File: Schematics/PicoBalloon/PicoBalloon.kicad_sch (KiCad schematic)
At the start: 31 parts, among them J2 SOLAR_L, J3 SOLAR_R, J4 LORA_ANT, J5 SWD, U1 STM32F103C8Tx, U3 TMP235A4DCKR

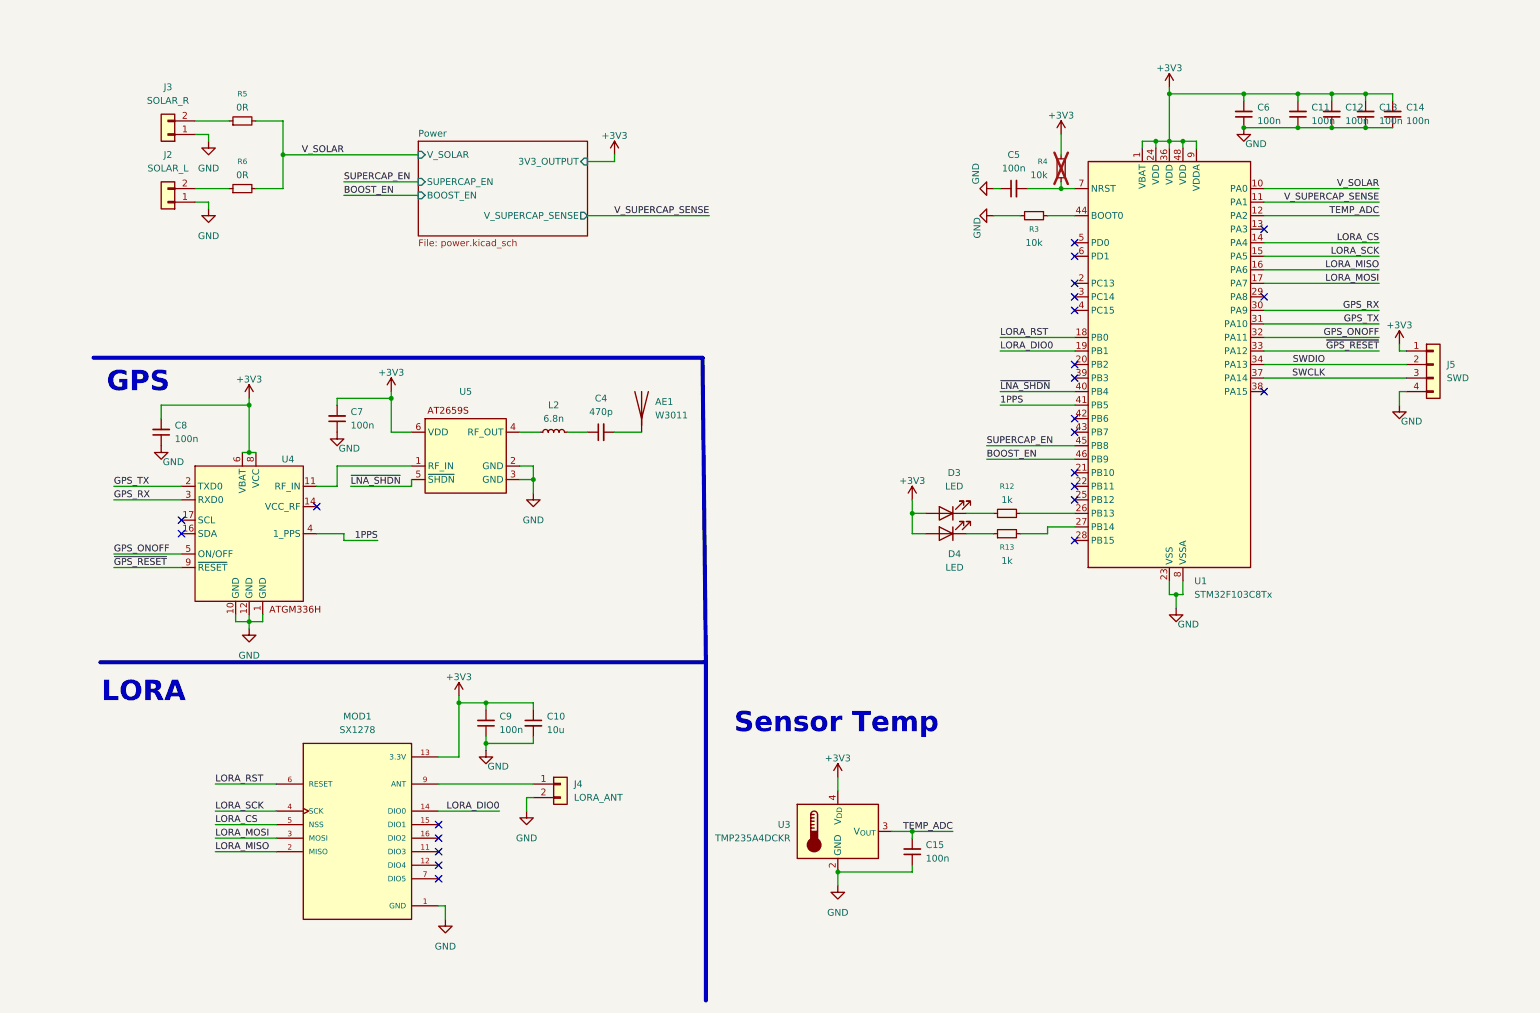
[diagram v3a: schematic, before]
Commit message: Updated R10 size and datasheets
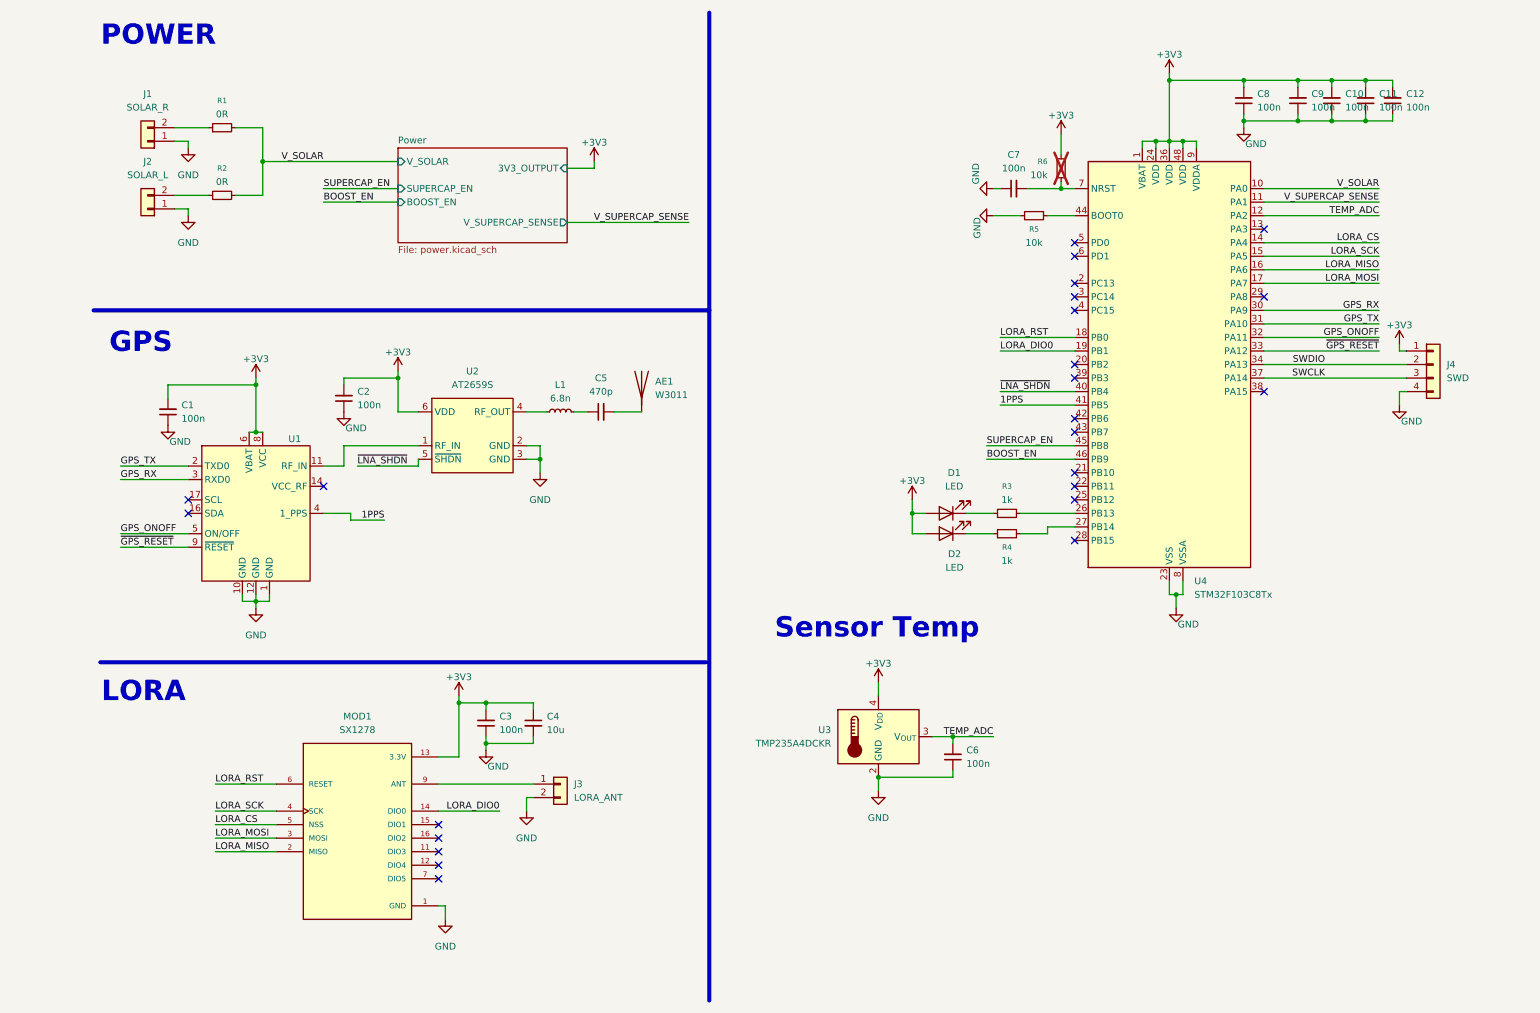
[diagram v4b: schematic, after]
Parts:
- removed U5: ~, symbol gluonLibrary:AT2659S
- added U2: AT2659S, Package_TO_SOT_SMD:SOT-23-6_Handsoldering, symbol gluonLibrary:AT2659S
- U1: renamed from U4; value ~ -> ATGM336H; footprint (none) -> GluonLib:ATGM336H; LCSC (none) -> https://lcsc.com/product-detail/GNSS-Modules_ZHONGKEWEI-ATG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
- renumbered C8 to C1, C12 to C10, C13 to C11, C14 to C12, C7 to C2, C9 to C3, C10 to C4, C4 to C5, C15 to C6, C5 to C7, C6 to C8, C11 to C9, D3 to D1, D4 to D2, J3 to J1, J4 to J3, J5 to J4, L2 to L1, R5 to R1, R6 to R2, R12 to R3, R13 to R4, R3 to R5, R4 to R6, U1 to U4
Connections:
- net +3V3: now also U2.6 (VDD)
- net GND: now also U2.2 (GND), U2.3 (GND)
- net ~{LNA_SHDN}: now also U2.5 (~{SHDN})
- net at U1.11 (RF_IN): now also U2.1 (RF_IN)
- net at L1.1: now also U2.4 (RF_OUT)
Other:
- note added: "POWER"
- moved on the sheet: AE1, C1, C10, C11, C12, C2, C5, C6, C8, C9, J1, J2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

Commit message: Fixed footprints and schematic symbols
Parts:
- removed AE1: W3011, RF_Antenna:Pulse_W3011, symbol Device:Antenna
- added AE1: Antenna_Chip, RF_Antenna:Pulse_W3011, symbol Device:Antenna_Chip
- MOD1: footprint GluonLib:SX1278_XCVR_RFM98W-433S2 -> GluonLib:SX1278
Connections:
- net GND: now also AE1.1 (FEED)
- net at C5.2: now also AE1.2 (PCB_Trace)
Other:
- note added: "Temp Sensor"
- note removed: "Sensor Temp"
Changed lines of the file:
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@@
 	(generator_version "9.0")
 	(paper "A4")
-	(text "Sensor Temp"
+	(text "Temp Sensor"
 		(exclude_from_sim no)
 		(at 158.496 128.27 0)
@@
 	(wire
 		(pts
+			(xy 119.38 87.63) (xy 119.38 88.9)
+		)
+		(stroke
+			(width 0)
+			(type default)
+		)
+	)
+	(wire
+		(pts
 			(xy 92.71 162.56) (xy 92.71 160.02)
 		)
@@
 	)
 	(symbol
+		(lib_id "Device:Antenna_Chip")
+		(at 116.84 85.09 0)
+		(mirror y)
+		(unit 1)
+		(exclude_from_sim no)
+		(in_bom yes)
+		(on_board yes)
+		(dnp no)
+		(fields_autoplaced yes)
+		(property "Reference" "AE1"
+			(at 116.205 73.66 0)
+			(effects
+				(font
+					(size 1.27 1.27)
+				)
+			)
+		)
+		(property "Value" "Antenna_Chip"
+			(at 116.205 76.2 0)
+			(effects
+				(font
+					(size 1.27 1.27)
+				)
+			)
+		)
+		(property "Footprint" "RF_Antenna:Pulse_W3011"
+			(at 119.38 80.645 0)
+			(effects
+				(font
+					(size 1.27 1.27)
+				)
+				(hide yes)
+			)
+		)
+		(property "Datasheet" "~"
+			(at 119.38 80.645 0)
+			(effects
+				(font
+					(size 1.27 1.27)
+				)
+				(hide yes)
+			)
+		)
+		(property "Description" "Ceramic chip antenna with pin for PCB trace"
+			(at 116.84 85.09 0)
+			(effects
+				(font
+					(size 1.27 1.27)
+				)
+				(hide yes)
+			)
+		)
+		(property "LCSC" "https://lcsc.com/product-detail/Antennas_PULSE-W3011_C6604735.html"
+			(at 116.84 85.09 0)
+			(effects
+				(font
+					(size 1.27 1.27)
+				)
+				(hide yes)
+			)
+		)
+		(pin "1"
+		)
+		(pin "2"
+		)
+		(instances
+			(project ""
+				(path "/0b983980-f4cd-49d3-aecb-9bdb75de805b"
+					(reference "AE1")
+					(unit 1)
+				)
+			)
+		)
+	)
+	(symbol
 		(lib_id "power:GND")
 		(at 95.25 99.06 0)
@@
 	)
 	(symbol
+		(lib_id "power:GND")
+		(at 119.38 88.9 0)
+		(unit 1)
+		(exclude_from_sim no)
+		(in_bom yes)
+		(on_board yes)
+		(dnp no)
+		(fields_autoplaced yes)
+		(property "Reference" "#PWR031"
+			(at 119.38 95.25 0)
+			(effects
+				(font
+					(size 1.27 1.27)
+				)
+				(hide yes)
+			)
+		)
+		(property "Value" "GND"
+			(at 119.38 93.98 0)
+			(effects
+				(font
+					(size 1.27 1.27)
+				)
+			)
+		)
+		(property "Footprint" ""
+			(at 119.38 88.9 0)
+			(effects
+				(font
+					(size 1.27 1.27)
+				)
+				(hide yes)
+			)
+		)
+		(property "Datasheet" ""
+			(at 119.38 88.9 0)
+			(effects
+				(font
+					(size 1.27 1.27)
+				)
+				(hide yes)
+			)
+		)
+		(property "Description" "Power symbol creates a global label with name \"GND\" , ground"
+			(at 119.38 88.9 0)
+			(effects
+				(font
+					(size 1.27 1.27)
+				)
+				(hide yes)
+			)
+		)
+		(pin "1"
+		)
+		(instances
+			(project "PicoBalloon"
+				(path "/0b983980-f4cd-49d3-aecb-9bdb75de805b"
+					(reference "#PWR031")
+					(unit 1)
+				)
+			)
+		)
+	)
+	(symbol
 		(lib_id "Device:C_Small")
 		(at 106.68 87.63 90)
@@
 			)
 		)
-		(property "Footprint" "GluonLib:SX1278_XCVR_RFM98W-433S2"
+		(property "Footprint" "GluonLib:SX1278"
 			(at 60.96 167.64 0)
 			(effects
@@
 					(unit 1)
 				)
-			)
-		)
-	)
-	(symbol
-		(lib_id "Device:Antenna")
-		(at 114.3 82.55 0)
-		(unit 1)
-		(exclude_from_sim no)
-		(in_bom yes)
-		(on_board yes)
-		(dnp no)
-		(fields_autoplaced yes)
-		(property "Reference" "AE1"
-			(at 116.84 81.9149 0)
-			(effects
-				(font
-					(size 1.27 1.27)
-				)
-				(justify left)
-			)
-		)
-		(property "Value" "W3011"
-			(at 116.84 84.4549 0)
-			(effects
-				(font
-					(size 1.27 1.27)
-				)
-				(justify left)
-			)
-		)
-		(property "Footprint" "RF_Antenna:Pulse_W3011"
-			(at 114.3 82.55 0)
-			(effects
-				(font
-					(size 1.27 1.27)
-				)
-				(hide yes)
-			)
-		)
-		(property "Datasheet" "~"
-			(at 114.3 82.55 0)
-			(effects
-				(font
-					(size 1.27 1.27)
-				)
-				(hide yes)
-			)
-		)
-		(property "Description" "Antenna"
-			(at 114.3 82.55 0)
-			(effects
-				(font
-					(size 1.27 1.27)
-				)
-				(hide yes)
-			)
-		)
-		(property "LCSC" "https://lcsc.com/product-detail/Antennas_PULSE-W3011_C6604735.html"
-			(at 114.3 82.55 0)
-			(effects
-				(font
-					(size 1.27 1.27)
-				)
-				(hide yes)
-			)
-		)
-		(pin "1"
-		)
-		(instances
-			(project ""
-				(path "/0b983980-f4cd-49d3-aecb-9bdb75de805b"
-					(reference "AE1")
-					(unit 1)
-				)

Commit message: First PCB layout
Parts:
- J1, J2: footprint Connector_PinHeader_2.00mm:PinHeader_1x02_P2.00mm_Vertical -> GluonLib:2_PAD_SMD
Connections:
- net GND: now also AE1.2 (PCB_Trace); no longer AE1.1 (FEED)
- net at C5.2: now also AE1.1 (FEED); no longer AE1.2 (PCB_Trace)
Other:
- company: (none) -> Laboratorio Gluon
- title: (none) -> Picoballoon v1
- moved on the sheet: AE1
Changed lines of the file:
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@@
 	(generator_version "9.0")
 	(paper "A4")
+	(title_block
+		(title "Picoballoon v1")
+		(date "2025-07-29")
+		(company "Laboratorio Gluon")
+	)
 	(text "Temp Sensor"
 		(exclude_from_sim no)
@@
 		(lib_id "Device:Antenna_Chip")
 		(at 116.84 85.09 0)
-		(mirror y)
 		(unit 1)
 		(exclude_from_sim no)
@@
 		(on_board yes)
 		(dnp no)
-		(fields_autoplaced yes)
 		(property "Reference" "AE1"
-			(at 116.205 73.66 0)
+			(at 117.475 73.66 0)
 			(effects
 				(font
@@
 		)
 		(property "Value" "Antenna_Chip"
-			(at 116.205 76.2 0)
+			(at 117.475 76.2 0)
 			(effects
 				(font
@@
 		)
 		(property "Footprint" "RF_Antenna:Pulse_W3011"
-			(at 119.38 80.645 0)
+			(at 114.3 80.645 0)
 			(effects
 				(font
@@
 		)
 		(property "Datasheet" "~"
-			(at 119.38 80.645 0)
+			(at 114.3 80.645 0)
 			(effects
 				(font
@@
 			)
 		)
-		(property "Footprint" "Connector_PinHeader_2.00mm:PinHeader_1x02_P2.00mm_Vertical"
+		(property "Footprint" "GluonLib:2_PAD_SMD"
 			(at 21.59 49.53 0)
 			(effects
@@
 			)
 		)
-		(property "Footprint" "Connector_PinHeader_2.00mm:PinHeader_1x02_P2.00mm_Vertical"
+		(property "Footprint" "GluonLib:2_PAD_SMD"
 			(at 21.59 36.83 0)
 			(effects

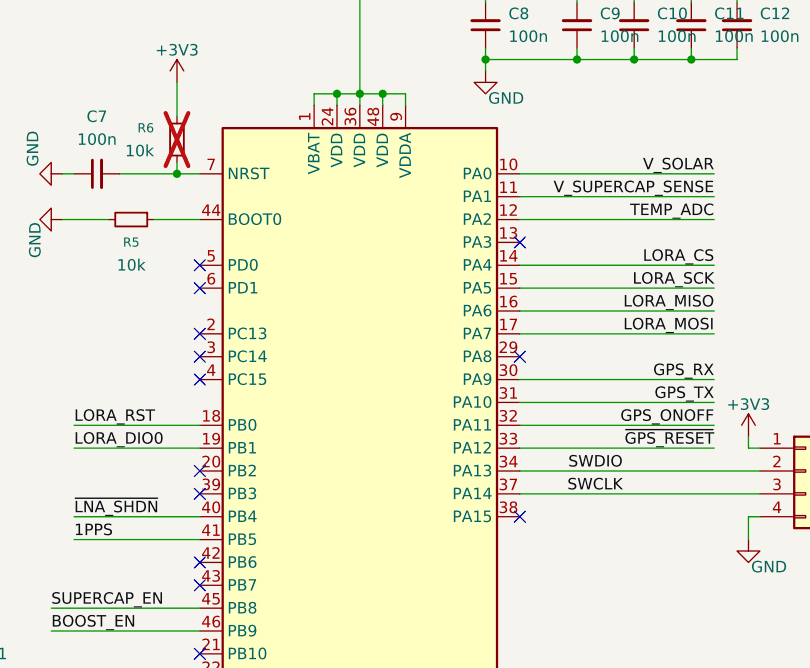
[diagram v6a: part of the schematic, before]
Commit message: Version 1.0 provisional de la PCB
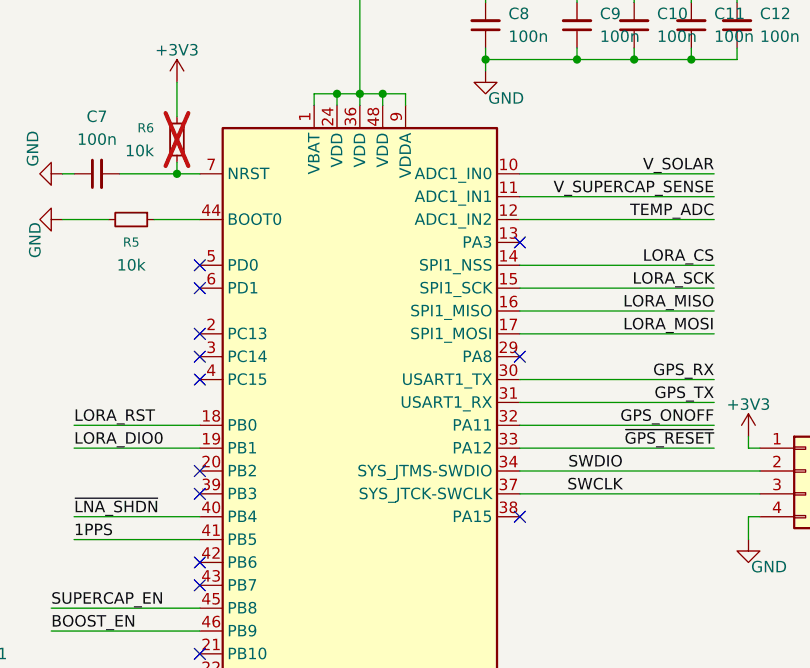
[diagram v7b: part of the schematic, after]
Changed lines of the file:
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@@
 			)
 		)
-		(property "Datasheet" "~"
+		(property "Datasheet" "https://lcsc.com/datasheet/lcsc_datasheet_2410311328_PULSE-W3011_C6604735.pdf"
 			(at 114.3 80.645 0)
 			(effects
@@
 		)
 		(pin "37"
+			(alternate "SYS_JTCK-SWCLK")
 		)
 		(pin "33"
 		)
 		(pin "34"
+			(alternate "SYS_JTMS-SWDIO")
 		)
 		(pin "38"
@@
 		)
 		(pin "12"
+			(alternate "ADC1_IN2")
 		)
 		(pin "9"
 		)
 		(pin "11"
+			(alternate "ADC1_IN1")
 		)
 		(pin "10"
+			(alternate "ADC1_IN0")
 		)
 		(pin "44"
@@
 		)
 		(pin "14"
+			(alternate "SPI1_NSS")
 		)
 		(pin "46"
@@
 		)
 		(pin "30"
+			(alternate "USART1_TX")
 		)
 		(pin "48"
@@
 		)
 		(pin "17"
+			(alternate "SPI1_MOSI")
 		)
 		(pin "13"
 		)
 		(pin "15"
+			(alternate "SPI1_SCK")
 		)
 		(pin "31"
+			(alternate "USART1_RX")
 		)
 		(pin "16"
+			(alternate "SPI1_MISO")
 		)
 		(instances

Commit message: Started working on PCB A1.1
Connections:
- net at U1.11 (RF_IN): now also U2.4 (RF_OUT); no longer U2.1 (RF_IN)
- net at L1.1: now also U2.1 (RF_IN); no longer U2.4 (RF_OUT)
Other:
- title: Picoballoon v1 -> Picoballoon A.1.1
- moved on the sheet: AE1, C2, C5, L1, U2
